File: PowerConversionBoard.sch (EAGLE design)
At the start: 32 parts, among them Q1 6.5A/20V/35mΩ, U3 AZ1117EH-3.3TRG1

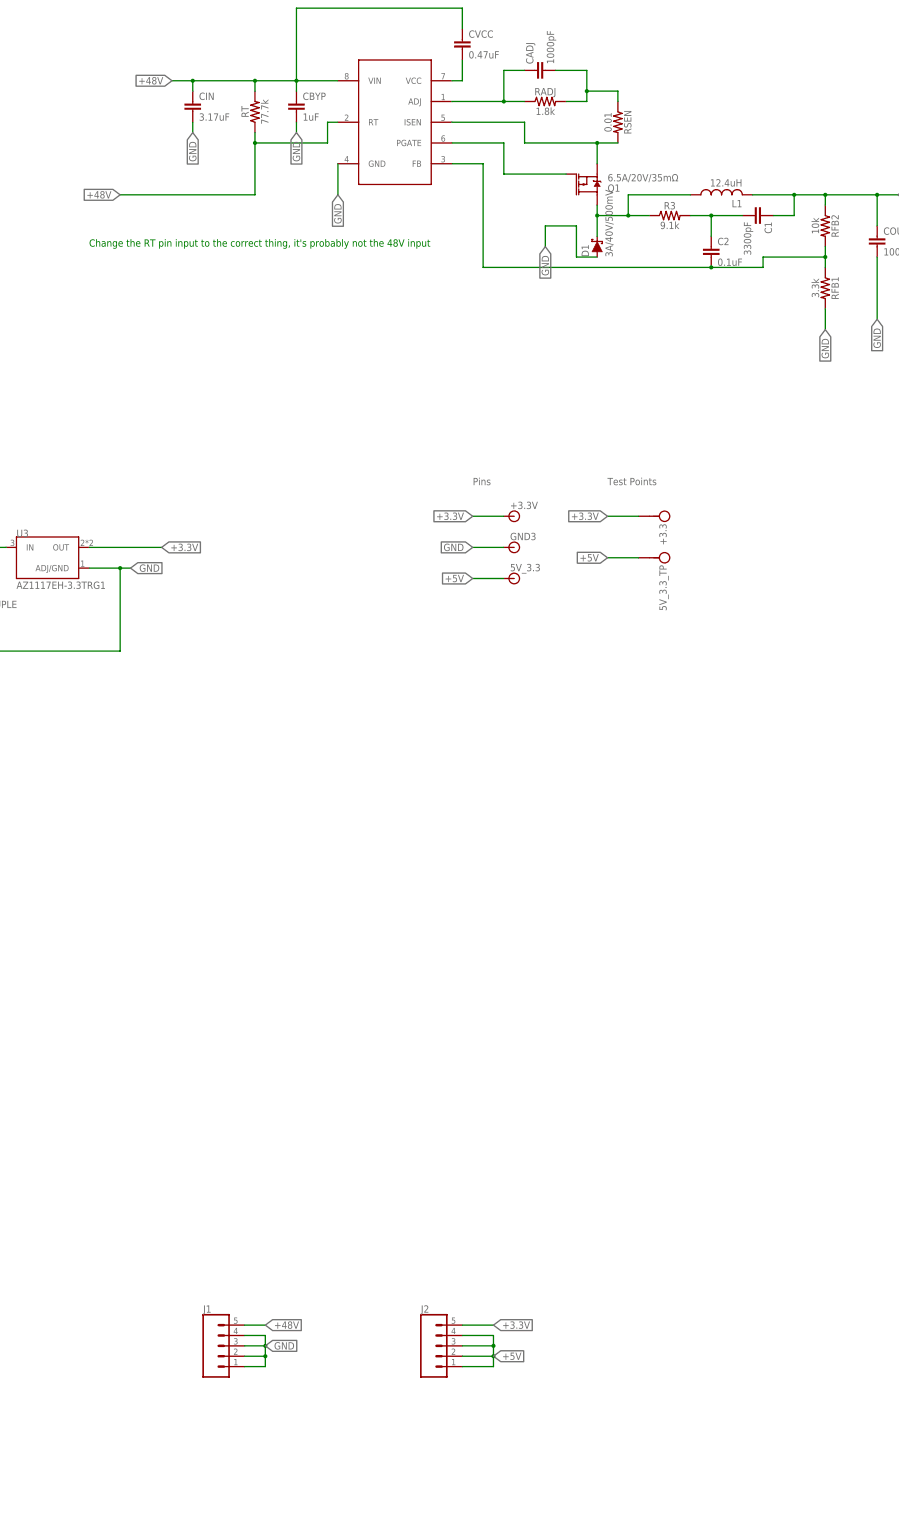
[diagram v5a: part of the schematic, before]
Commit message: Changed Buck Controller output to 5.2V (did not change net label); added RC Circuit to Linear regulator; added connection to distribution board
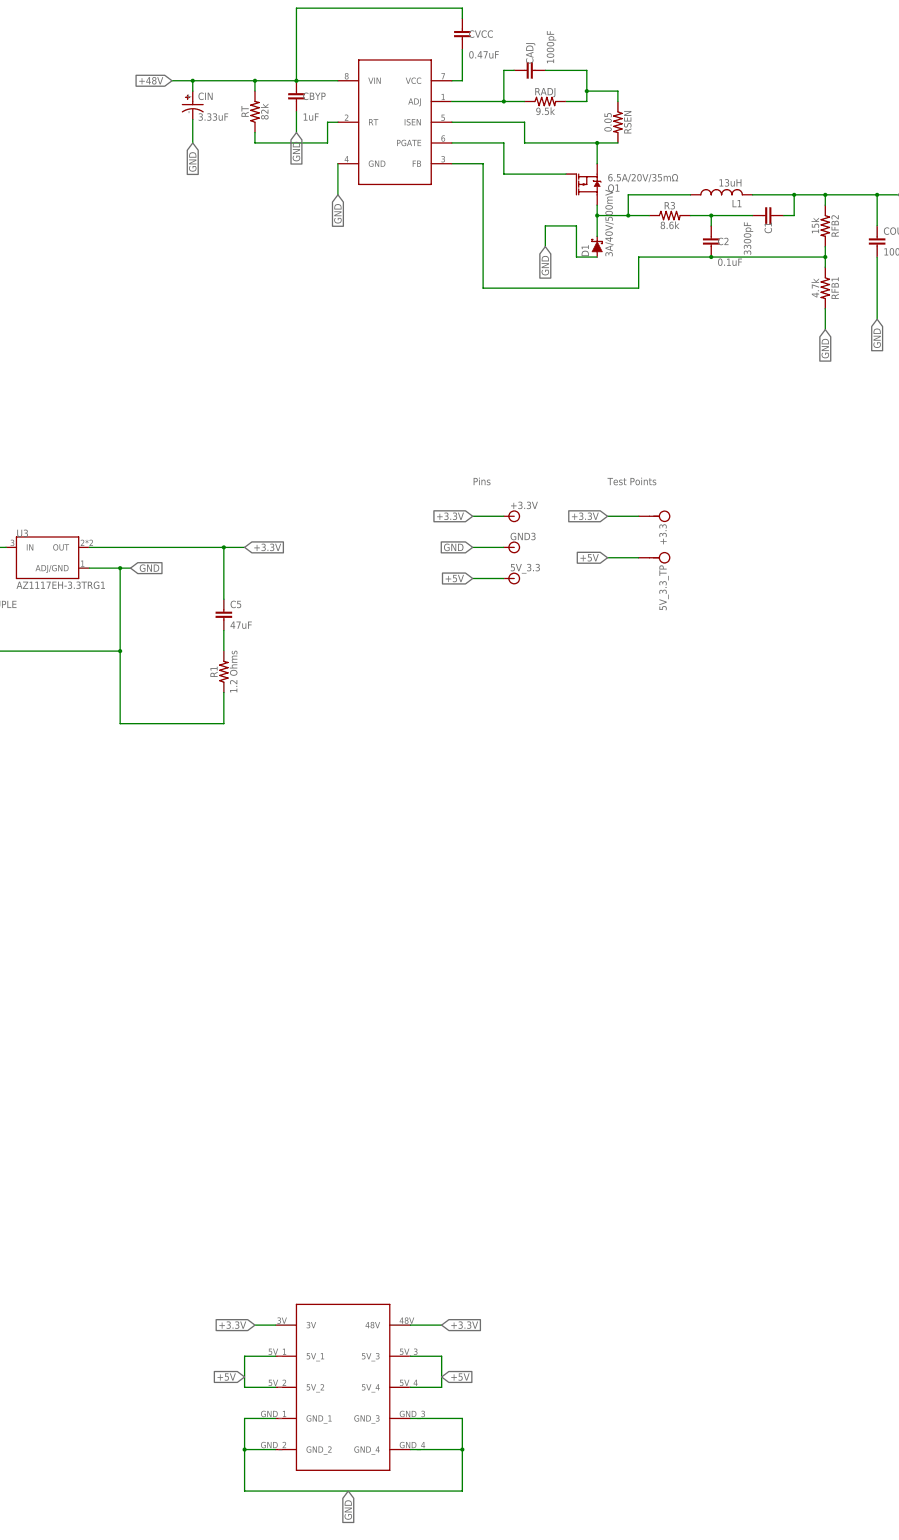
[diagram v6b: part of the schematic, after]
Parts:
- removed J1, J2: (no value), SparkFun-Connectors:CONN_05
- added C5: 47uF, SparkFun-Capacitors:0.1UF-0603-25V-5%
- added R1: 1.2 Ohms, SparkFun-Resistors:1.6KOHM-0603-1/10W-1%
- added U$2: DIST_TO_CONV, Dist_To_Conv_Connector:DIST_TO_CONV
- C1, C2: device Nordic_nRF:CAPACITOR_0201_M -> SparkFun-Capacitors:12PF-0603-50V-5%
- CADJ, CVCC: device Nordic_nRF:CAPACITOR_0201_M -> SparkFun-Capacitors:5.6PF-0603-50V-5%
- CBYP: device Nordic_nRF:CAPACITOR_0201_M -> SparkFun-Capacitors:3.3NF-0603-100V-10%
- CIN: value 3.17uF -> 3.33uF; device Nordic_nRF:CAPACITOR_0201_M -> brick-capacitor-UCM1H331MNL1GS:UCM1H331MNL1GS
- L1: value 12.4uH -> 13uH
- R3: value 9.1k -> 8.6k
- RADJ: value 1.8k -> 9.5k
- RFB1: value 3.3k -> 4.7k
- RFB2: value 10k -> 15k
- RSEN: value 0.01 -> 0.05
- RT: value 77.7k -> 82k; device SparkFun-Resistors:RESISTOR0603 -> SparkFun-Resistors:82OHM-0603-1/10W-1%
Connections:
- new net N$1: RT.1, U$1.RT
- new net N$12: C5.2, R1.2
- net +3.3V: now also C5.1, U$2.3V, U$2.48V; no longer J2.5
- net +48V: now also CIN.+; no longer CIN.1, J1.5, RT.1, U$1.RT
- net +5V: now also U$2.5V_1, U$2.5V_2, U$2.5V_3, U$2.5V_4; no longer J2.1, J2.2, J2.3, J2.4
- net GND: now also CIN.-, R1.1, U$2.GND_1, U$2.GND_2, U$2.GND_3, U$2.GND_4; no longer CIN.2, J1.1, J1.2, J1.3, J1.4
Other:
- note removed: "Change the RT pin input to the correct thing, it's probably not the 48V input"

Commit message: Copied in last year's capacitor and inductor
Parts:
- added C24: 150uF, PowerComponents:C-TANTALUM(10UF_150UF)
- added U$7: HCM1305, HCM1305:HCM1305
- D1: value 3A/40V/500mV -> DIODE-SCHOTTKY-B340A
- Q1: value 6.5A/20V/35mΩ -> MOSFET_PCH-NDS8434
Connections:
- removed net N$1: RT.1, U$1.RT
- net +48V: now also RT.1, U$1.RT
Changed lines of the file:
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@@
 <setting verticaltext="up"/>
 </settings>
-<grid distance="0.1" unitdist="inch" unit="inch" style="lines" multiple="1" display="no" altdistance="0.01" altunitdist="inch" altunit="inch"/>
+<grid distance="0.000000123031" unitdist="inch" unit="inch" style="lines" multiple="1" display="no" altdistance="0.01" altunitdist="inch" altunit="inch"/>
 <layers>
 <layer number="1" name="Top" color="4" fill="1" visible="no" active="no"/>
@@
 <part name="U$1" library="Buck_Controller" deviceset="LM5085" device=""/>
 <part name="COUPLE" library="SparkFun-Capacitors" library_urn="urn:adsk.eagle:library:510" deviceset="1.0NF/1000PF" device="-0603-50V-10%" package3d_urn="urn:adsk.eagle:package:37414/1" value="1nF"/>
-<part name="D1" library="SparkFun-DiscreteSemi" library_urn="urn:adsk.eagle:library:514" deviceset="DIODE-SCHOTTKY" device="-B340A" package3d_urn="urn:adsk.eagle:package:38443/1" value="3A/40V/500mV"/>
-<part name="Q1" library="SparkFun-DiscreteSemi" library_urn="urn:adsk.eagle:library:514" deviceset="MOSFET_PCH" device="-NDS8434" package3d_urn="urn:adsk.eagle:package:38445/1" value="6.5A/20V/35mΩ"/>
+<part name="D1" library="SparkFun-DiscreteSemi" library_urn="urn:adsk.eagle:library:514" deviceset="DIODE-SCHOTTKY" device="-B340A" package3d_urn="urn:adsk.eagle:package:38443/1" value=""/>
+<part name="Q1" library="SparkFun-DiscreteSemi" library_urn="urn:adsk.eagle:library:514" deviceset="MOSFET_PCH" device="-NDS8434" package3d_urn="urn:adsk.eagle:package:38445/1" value=""/>
 <part name="RFB1" library="SparkFun-Resistors" library_urn="urn:adsk.eagle:library:532" deviceset="RESISTOR" device="0603" package3d_urn="urn:adsk.eagle:package:39650/1" value="4.7k"/>
 <part name="RADJ" library="SparkFun-Resistors" library_urn="urn:adsk.eagle:library:532" deviceset="RESISTOR" device="0603" package3d_urn="urn:adsk.eagle:package:39650/1" value="9.5k"/>
@@
 <part name="CIN" library="brick-capacitor-UCM1H331MNL1GS" deviceset="UCM1H331MNL1GS" device="" package3d_urn="urn:adsk.eagle:package:24202090/2" value="3.33uF"/>
 <part name="R1" library="SparkFun-Resistors" library_urn="urn:adsk.eagle:library:532" deviceset="1.6KOHM" device="-0603-1/10W-1%" package3d_urn="urn:adsk.eagle:package:39650/1" value="1.2 Ohms"/>
+<part name="C24" library="PowerComponents" deviceset="C-TANTALUM(10UF_150UF)" device="" value="150uF"/>
+<part name="U$7" library="HCM1305" deviceset="HCM1305" device=""/>
 </parts>
 <sheets>
@@
 <attribute name="NAME" x="150.876" y="60.96" size="1.778" layer="95" font="vector" rot="R90" align="bottom-center"/>
 <attribute name="VALUE" x="153.924" y="60.96" size="1.778" layer="96" font="vector" rot="R90" align="top-center"/>
+</instance>
+<instance part="C24" gate="G$1" x="329.438" y="157.48" smashed="yes">
+<attribute name="NAME" x="330.454" y="158.115" size="1.778" layer="95"/>
+<attribute name="VALUE" x="330.454" y="153.289" size="1.778" layer="96"/>
+</instance>
+<instance part="U$7" gate="G$1" x="273.232953125" y="185.944271875" smashed="yes" rot="R90">
+<attribute name="NAME" x="268.137334375" y="188.49208125" size="1.78346875" layer="95"/>
 </instance>
 </instances>
@@
 <pinref part="CIN" gate="G$1" pin="+"/>
 </segment>
+<segment>
+<pinref part="U$1" gate="G$1" pin="RT"/>
+<wire x1="180.34" y1="195.58" x2="177.8" y2="195.58" width="0.1524" layer="91"/>
+<wire x1="177.8" y1="195.58" x2="177.8" y2="190.5" width="0.1524" layer="91"/>
+<wire x1="177.8" y1="190.5" x2="160.02" y2="190.5" width="0.1524" layer="91"/>
+<wire x1="160.02" y1="190.5" x2="160.02" y2="193.04" width="0.1524" layer="91"/>
+<pinref part="RT" gate="G$1" pin="1"/>
+<label x="160.02" y="190.5" size="1.778" layer="95" rot="R270" xref="yes"/>
+</segment>
 </net>
 <net name="N$3" class="0">
@@
 </segment>
 </net>
-<net name="N$1" class="0">
-<segment>
-<pinref part="U$1" gate="G$1" pin="RT"/>
-<wire x1="180.34" y1="195.58" x2="177.8" y2="195.58" width="0.1524" layer="91"/>
-<wire x1="177.8" y1="195.58" x2="177.8" y2="190.5" width="0.1524" layer="91"/>
-<wire x1="177.8" y1="190.5" x2="160.02" y2="190.5" width="0.1524" layer="91"/>
-<wire x1="160.02" y1="190.5" x2="160.02" y2="193.04" width="0.1524" layer="91"/>
-<pinref part="RT" gate="G$1" pin="1"/>
-</segment>
-</net>

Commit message: copied old parts over
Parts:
- removed COUT: 100uF, Nordic_nRF:CAPACITOR_0201_M
- removed D1: DIODE-SCHOTTKY-B340A, SparkFun-DiscreteSemi:DIODE-SCHOTTKY-B340A
- removed L1: 13uH, Nordic_nRF:INDUCTOR_0201_M
- added U$4: SWITCHMODE_SCHOTTKY, PowerComponents:SWITCHMODE_SCHOTTKY
- CIN: value 3.33uF -> 47uF
- RSEN: value 0.05 -> 0.01; device SparkFun-Resistors:RESISTOR0603 -> INA4181A4:CSS2H-2512
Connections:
- removed net N$8: CADJ.2, RADJ.2, RSEN.1
- net +48V: now also CADJ.2, RADJ.2, RSEN.2
- net +5V: now also C24.+, U$7.2; no longer COUT.1, L1.2
- net GND: now also C24.-, U$4.P$1, U$4.P$3; no longer COUT.2, D1.A
- net N$10: now also U$4.P$4, U$7.1; no longer D1.C, L1.1
- net N$9: now also RSEN.1; no longer RSEN.2
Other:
- moved on the sheet: C24, CADJ, RADJ, U$7
